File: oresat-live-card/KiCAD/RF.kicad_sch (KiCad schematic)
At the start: 36 parts, among them J5 2X1_TH_JUMPER, J9 Conn_Coaxial, U19 TQP9111, U6 SN74LVC1G32QDBVRQ1, U8 MIC94090YC6-TR

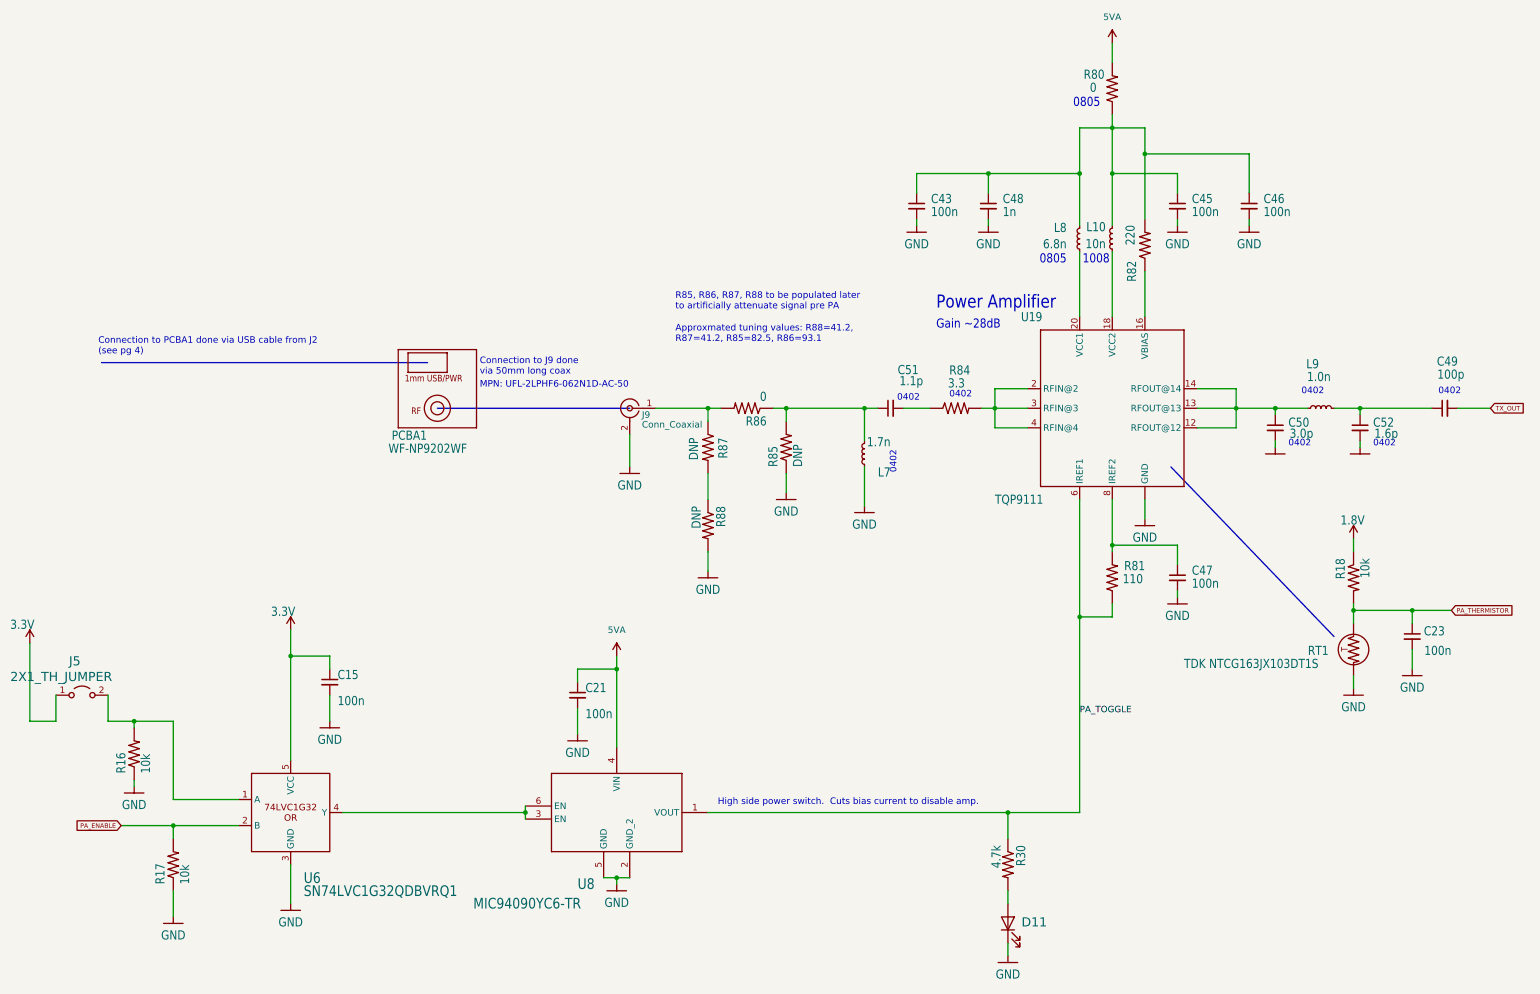
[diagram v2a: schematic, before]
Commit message: Upgraded to KiCAD 8.0. Added notes on U.FL cable and USB cables to wifi and camera.
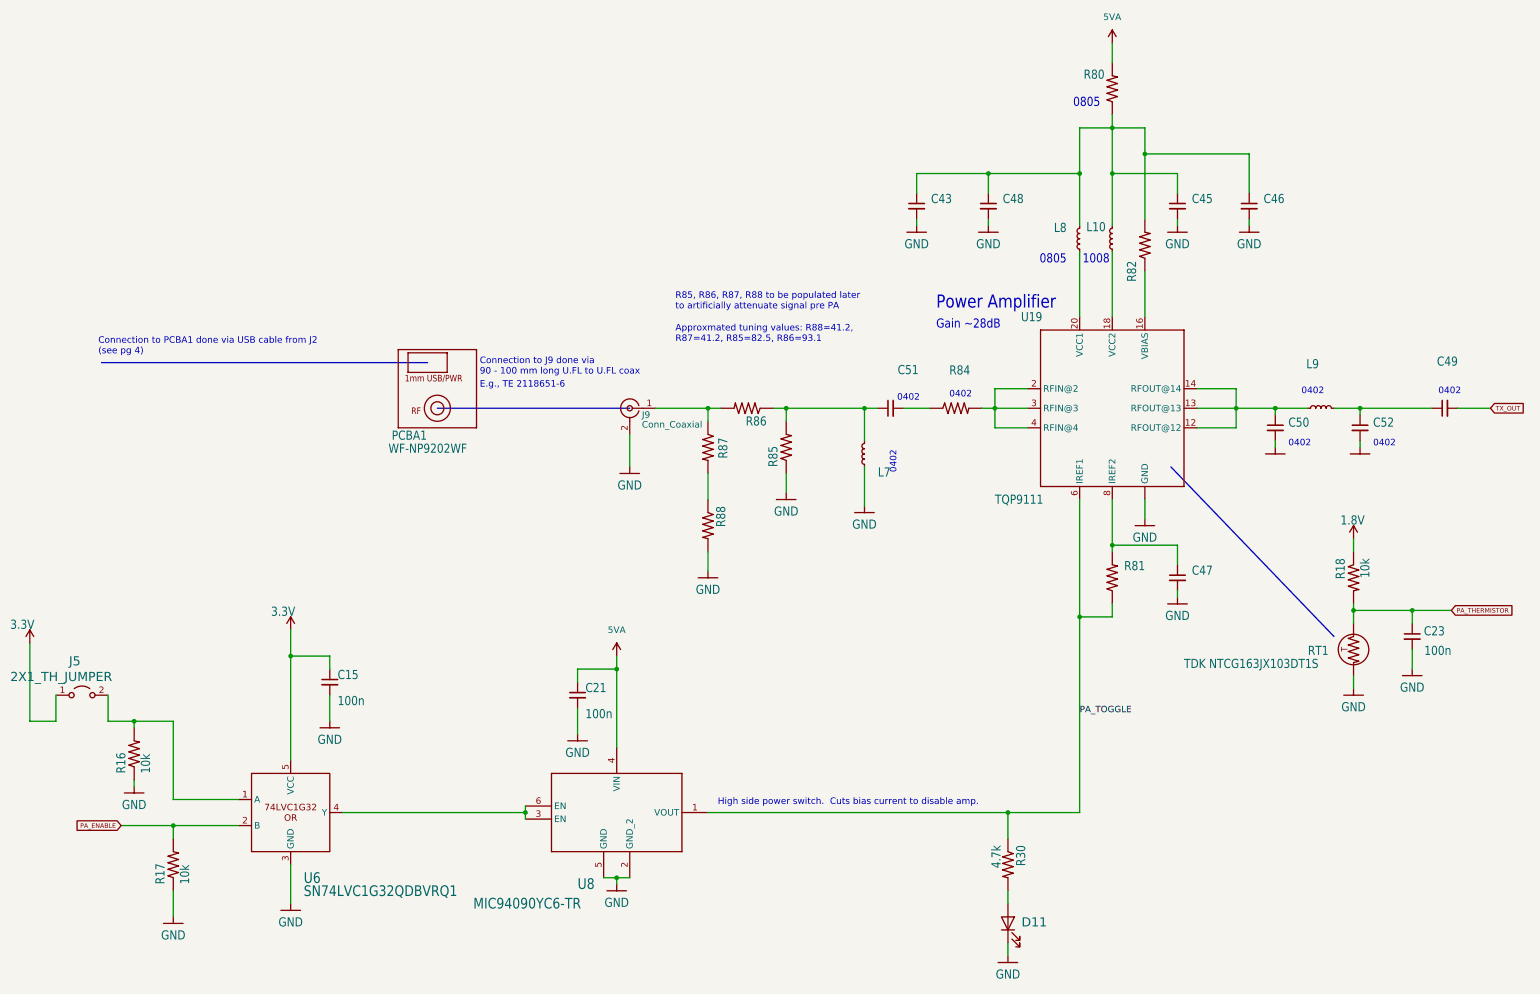
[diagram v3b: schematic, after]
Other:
- note added: "Connection to J9 done via 90 - 100 mm long U.FL to U.FL coax"
- note added: "E.g., TE 2118651-6"
- note removed: "Connection to J9 done via 50mm long coax"
- note removed: "MPN: UFL-2LPHF6-062N1D-AC-50"

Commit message: added new sheets for LNA and switching
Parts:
- removed C15, C21, C23: 100n, Resistor_SMD:R_0603_1608Metric, symbol Device:C_Small
- removed C43, C45, C46, C47: CGA2B1X7R1C104K050BC, Resistor_SMD:R_0603_1608Metric, symbol Device:C_Small
- removed C48: CGA2B2NP01H102J050BA, Resistor_SMD:R_0402_1005Metric, symbol Device:C_Small
- removed C49: GCM1885C1H101JA16D, Resistor_SMD:R_0402_1005Metric, symbol Device:C_Small
- removed C50: 04025U3R0BAT2A, Resistor_SMD:R_0402_1005Metric, symbol Device:C_Small
- removed C51: 04025J1R1PBSTR\500, Resistor_SMD:R_0402_1005Metric, symbol Device:C_Small
- removed C52: 04025U1R6BAT2A, Resistor_SMD:R_0402_1005Metric, symbol Device:C_Small
- removed D11: 150060VS55040, oresat-live-card:LED-0603, symbol Device:LED
- removed J5: 2X1_TH_JUMPER, oresat-live-card:2X1, symbol Jumper:Jumper_2_Open
- removed J9: Conn_Coaxial, Connector_Coaxial:U.FL_Molex_MCRF_73412-0110_Vertical, symbol Connector:Conn_Coaxial
- removed L10: Fixed Inductors 1008 10nH Unshld 5% 1.6A 60mOhms, oresat-live-card:INDC2928X203N, symbol Device:L_Small
- removed L7: 0402DC-1N7XJRU, Resistor_SMD:R_0402_1005Metric, symbol Device:L_Small
- removed L8: 0805CS-060XJLC, Resistor_SMD:R_0805_2012Metric, symbol Device:L_Small
- removed L9: MLK1005S1N0ST000, Resistor_SMD:R_0402_1005Metric, symbol Device:L_Small
- removed PCBA1: WF-NP9202WF, oresat-live-card:WF-NP9202, symbol oresat-live-card-eagle-import:WF-NP9202WF
- removed R16, R17, R18: 10k, Resistor_SMD:R_0603_1608Metric, symbol oresat-passives:R-US
- removed R30: 4.7k, Resistor_SMD:R_0603_1608Metric, symbol oresat-passives:R-US
- removed R80: ERJ-6GEY0R00V, Resistor_SMD:R_0805_2012Metric, symbol oresat-passives:R-US
- removed R81: ERJ-2RKF1100X, Resistor_SMD:R_0402_1005Metric, symbol oresat-passives:R-US
- removed R82: ERJ-3EKF2200V, Resistor_SMD:R_0603_1608Metric, symbol oresat-passives:R-US
- removed R84: CRCW04023R30FKED, Resistor_SMD:R_0402_1005Metric, symbol oresat-passives:R-US
- removed R85: ERJ-3EKF82R5V, Resistor_SMD:R_0603_1608Metric, symbol oresat-passives:R-US
- removed R86: ERJ-3EKF93R1V, Resistor_SMD:R_0603_1608Metric, symbol oresat-passives:R-US
- removed R87, R88: ERJ-3EKF41R2V, Resistor_SMD:R_0603_1608Metric, symbol oresat-passives:R-US
- removed RT1: TDK NTCG163JX103DT1S, oresat-live-card:0603-THERMISTOR-B, symbol oresat-passives:THERMISTOR
- removed U19: TQP9111, oresat-live-card:QFN50P400X400X102-21N, symbol oresat-ics:TQP9111
- removed U6: SN74LVC1G32QDBVRQ1, oresat-live-card:DBV5, symbol oresat-ics:SN74LVC1G32QDBVRQ1
- removed U8: MIC94090YC6-TR, oresat-live-card:SC-70-6_MCH, symbol oresat-ics:MIC94090YC6-TR
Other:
- note removed: "0402"
- note removed: "0805"
- note removed: "1008"
- note removed: "Approxmated tuning values: R88=41.2, R87=41.2, R85=82.5, R86=93.1"
- note removed: "Connection to J9 done via 90 - 100 mm long U.FL to U.FL coax"
- note removed: "Connection to PCBA1 done via USB cable from J2 (see pg 4)"
- note removed: "E.g., TE 2118651-6"
- note removed: "Gain ~28dB"
- note removed: "High side power switch. Cuts bias current to disable amp."
- note removed: "Power Amplifier"
- note removed: "R85, R86, R87, R88 to be populated later to artificially attenuate signal pre PA"
- title: Oresat DxWifi Card -> (none)
